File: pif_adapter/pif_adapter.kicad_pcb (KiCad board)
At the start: 2 copper layers, 11 x 22 mm, 11 parts, among them P1 Conn_02x20_Odd_Even, P10 Conn_01x01, P11 Conn_01x01, P2 PIF-NUS, P3 Conn_01x01, P4 Conn_01x01, P5 Conn_01x01, P6 Conn_01x01, P7 Conn_01x01, P8 Conn_01x01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

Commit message: - updated revision infos - changed some traces
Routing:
- net GND: track 51.8 -> 51.1 mm
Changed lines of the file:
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@@
     (thickness 1.6)
     (drawings 20)
-    (tracks 221)
+    (tracks 222)
     (zones 0)
     (modules 11)
@@
   )
   (page A4)
+  (title_block
+    (title "UltraPIF Adapter")
+    (date 2020-03-04)
+    (rev 3)
+  )
   (layers
     (0 F.Cu signal)
@@
   )
   (setup
-    (last_trace_width 0.8)
+    (last_trace_width 0.4)
     (user_trace_width 0.4)
     (user_trace_width 0.8)
@@
   (segment (start 143.03 109.25) (end 142.12 108.34) (width 0.15) (layer F.Cu) (net 9))
   (segment (start 141.01 111.225) (end 141 111.215) (width 0.15) (layer F.Cu) (net 10))
-  (segment (start 143.975 110.75) (end 142.8 110.75) (width 0.15) (layer F.Cu) (net 10))
   (segment (start 141 111.215) (end 142.035 111.215) (width 0.4) (layer F.Cu) (net 10))
   (segment (start 142.5 110.75) (end 142.8 110.75) (width 0.4) (layer F.Cu) (net 10))
   (segment (start 142.035 111.215) (end 142.5 110.75) (width 0.4) (layer F.Cu) (net 10))
-  (segment (start 143.975 108.75) (end 144.925 108.75) (width 0.15) (layer F.Cu) (net 10))
   (via (at 146.5 102.3) (size 0.6) (drill 0.4) (layers F.Cu B.Cu) (net 10))
   (segment (start 145.2 102.3) (end 146.5 102.3) (width 0.4) (layer B.Cu) (net 10))
@@
   (segment (start 143.975 103.25) (end 144.8 103.25) (width 0.15) (layer F.Cu) (net 10))
   (segment (start 145.2 102.85) (end 145.2 102.3) (width 0.15) (layer F.Cu) (net 10))
-  (segment (start 143.975 110.75) (end 145.1 110.75) (width 0.15) (layer F.Cu) (net 10))
-  (segment (start 145.1 111.25) (end 144.6 111.75) (width 0.15) (layer F.Cu) (net 10))
-  (segment (start 145.1 111.1) (end 145.1 111.25) (width 0.15) (layer F.Cu) (net 10))
-  (segment (start 144.6 111.75) (end 143.975 111.75) (width 0.15) (layer F.Cu) (net 10))
-  (segment (start 147.2 102.3) (end 146.5 102.3) (width 0.4) (layer F.Cu) (net 10))
   (segment (start 141.785 108.675) (end 142.78 109.67) (width 0.4) (layer F.Cu) (net 10))
   (segment (start 141 108.675) (end 141.785 108.675) (width 0.4) (layer F.Cu) (net 10))
-  (segment (start 142.86 109.75) (end 142.78 109.67) (width 0.15) (layer F.Cu) (net 10))
-  (segment (start 143.925 109.75) (end 142.86 109.75) (width 0.15) (layer F.Cu) (net 10))
-  (segment (start 144.75 109.75) (end 145.1 109.75) (width 0.15) (layer F.Cu) (net 10))
-  (segment (start 143.925 109.75) (end 144.75 109.75) (width 0.15) (layer F.Cu) (net 10))
   (segment (start 141.005 113.76) (end 141 113.755) (width 0.4) (layer F.Cu) (net 10))
   (segment (start 142.91 112.53) (end 141.68 113.76) (width 0.4) (layer F.Cu) (net 10))
@@
   (segment (start 142.91 112.53) (end 142.91 112.08) (width 0.4) (layer F.Cu) (net 10))
   (segment (start 142.91 112.08) (end 142.91 111.84) (width 0.15) (layer F.Cu) (net 10))
-  (segment (start 147.2 104.1) (end 145.2 104.1) (width 0.4) (layer F.Cu) (net 10))
-  (segment (start 147.212501 104.087499) (end 147.2 104.1) (width 0.4) (layer F.Cu) (net 10))
   (segment (start 145.2 104.1) (end 145.4 104.1) (width 0.15) (layer F.Cu) (net 10))
   (segment (start 143.975 104.25) (end 145.05 104.25) (width 0.15) (layer F.Cu) (net 10))
   (segment (start 145.05 104.25) (end 145.2 104.1) (width 0.15) (layer F.Cu) (net 10))
-  (segment (start 147.2 102.3) (end 147.212501 102.312501) (width 0.4) (layer F.Cu) (net 10))
   (segment (start 146.5 102.3) (end 146.5 100.1) (width 0.4) (layer F.Cu) (net 10))
   (segment (start 146.5 96.92) (end 146.5 100.1) (width 0.8) (layer F.Cu) (net 10))
   (segment (start 148 96.7) (end 146.72 96.7) (width 0.8) (layer F.Cu) (net 10))
   (segment (start 146.72 96.7) (end 146.5 96.92) (width 0.8) (layer F.Cu) (net 10))
-  (segment (start 144.02 98.21) (end 144.02 95.92501) (width 0.4) (layer F.Cu) (net 10))
-  (segment (start 143.875 98.355) (end 144.02 98.21) (width 0.4) (layer F.Cu) (net 10))
-  (segment (start 143.875 101.655) (end 143.875 98.355) (width 0.4) (layer F.Cu) (net 10))
   (segment (start 143.875 101.655) (end 143.875 102.25) (width 0.15) (layer F.Cu) (net 10))
   (segment (start 144.985 101.655) (end 145.2 101.87) (width 0.4) (layer F.Cu) (net 10))
   (segment (start 143.875 101.655) (end 144.985 101.655) (width 0.4) (layer F.Cu) (net 10))
   (segment (start 145.2 101.87) (end 145.2 102.33) (width 0.4) (layer F.Cu) (net 10))
-  (segment (start 147.175 106.835) (end 145.1 108.91) (width 0.8) (layer F.Cu) (net 10))
-  (segment (start 147.175 102.225) (end 147.175 106.835) (width 0.8) (layer F.Cu) (net 10))
-  (segment (start 146.5 100.1) (end 146.5 101.55) (width 0.8) (layer F.Cu) (net 10))
-  (segment (start 145.1 108.91) (end 145.1 110.88) (width 0.8) (layer F.Cu) (net 10))
-  (segment (start 146.5 101.55) (end 147.175 102.225) (width 0.8) (layer F.Cu) (net 10))
+  (segment (start 145.1 110.75) (end 143.975 110.75) (width 0.15) (layer F.Cu) (net 10))
+  (segment (start 143.975 110.75) (end 142.8 110.75) (width 0.15) (layer F.Cu) (net 10))
+  (segment (start 145.5 110.75) (end 145.68 110.57) (width 0.15) (layer F.Cu) (net 10))
+  (segment (start 145.1 110.75) (end 145.5 110.75) (width 0.15) (layer F.Cu) (net 10))
+  (segment (start 145.68 108.63) (end 145.68 109.78) (width 0.4) (layer F.Cu) (net 10))
+  (segment (start 145.68 109.78) (end 145.68 110.57) (width 0.4) (layer F.Cu) (net 10))
+  (segment (start 142.86 109.75) (end 142.78 109.67) (width 0.15) (layer F.Cu) (net 10))
+  (segment (start 145.68 109.78) (end 145.65 109.75) (width 0.15) (layer F.Cu) (net 10))
+  (segment (start 145.65 109.75) (end 142.86 109.75) (width 0.15) (layer F.Cu) (net 10))
+  (segment (start 145.56 108.75) (end 145.68 108.63) (width 0.15) (layer F.Cu) (net 10))
+  (segment (start 143.975 108.75) (end 145.56 108.75) (width 0.15) (layer F.Cu) (net 10))
+  (segment (start 145.48 110.87) (end 145.48 110.77) (width 0.15) (layer F.Cu) (net 10))
+  (segment (start 143.975 111.75) (end 144.6 111.75) (width 0.15) (layer F.Cu) (net 10))
+  (segment (start 144.6 111.75) (end 145.48 110.87) (width 0.15) (layer F.Cu) (net 10))
+  (segment (start 145.68 110.57) (end 145.48 110.77) (width 0.4) (layer F.Cu) (net 10))
+  (segment (start 147.17 104.1) (end 145.2 104.1) (width 0.4) (layer F.Cu) (net 10))
+  (segment (start 147.175 104.105) (end 147.17 104.1) (width 0.4) (layer F.Cu) (net 10))
+  (segment (start 147.175 107.135) (end 145.68 108.63) (width 0.4) (layer F.Cu) (net 10))
+  (segment (start 146.5 102.3) (end 147.175 102.975) (width 0.4) (layer F.Cu) (net 10))
+  (segment (start 147.175 102.975) (end 147.175 107.135) (width 0.4) (layer F.Cu) (net 10))
+  (segment (start 143.875 98.355) (end 144.02 98.21) (width 0.4) (layer F.Cu) (net 10))
+  (segment (start 143.875 101.655) (end 143.875 98.355) (width 0.4) (layer F.Cu) (net 10))
+  (segment (start 144.02 98.21) (end 144.02 95.92501) (width 0.4) (layer F.Cu) (net 10))
   (segment (start 141.85 109.95) (end 141.005 109.95) (width 0.15) (layer F.Cu) (net 11))
   (segment (start 141.005 109.95) (end 141 109.945) (width 0.15) (layer F.Cu) (net 11))

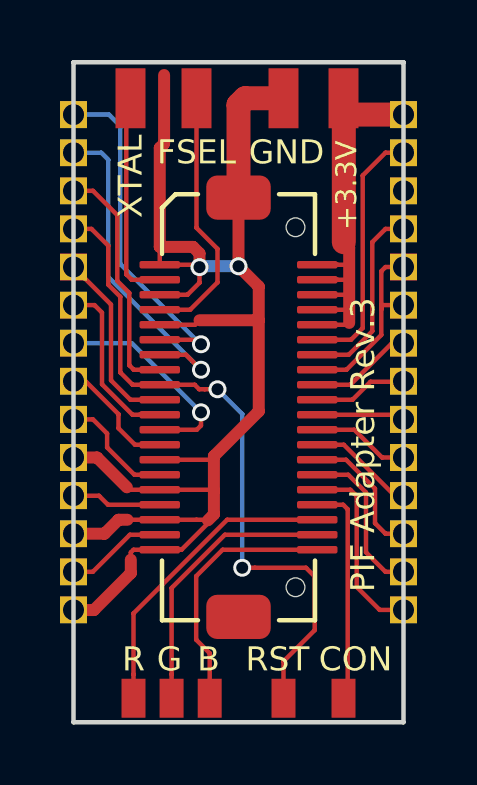
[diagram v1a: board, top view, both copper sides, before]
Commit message: improved ground trace
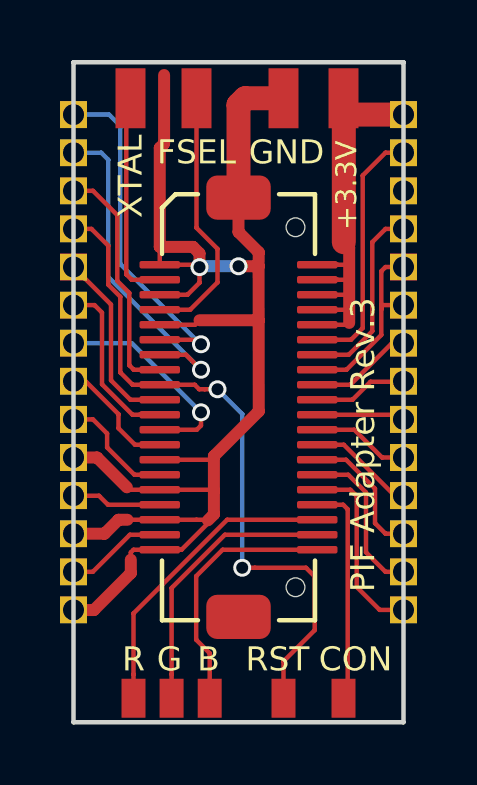
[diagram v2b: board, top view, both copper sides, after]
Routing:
- net GND: track 51.1 -> 51.8 mm
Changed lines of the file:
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@@
     (thickness 1.6)
     (drawings 20)
-    (tracks 222)
+    (tracks 224)
     (zones 0)
     (modules 11)
@@
   (segment (start 143.975 104.25) (end 145.05 104.25) (width 0.15) (layer F.Cu) (net 10))
   (segment (start 145.05 104.25) (end 145.2 104.1) (width 0.15) (layer F.Cu) (net 10))
-  (segment (start 146.5 102.3) (end 146.5 100.1) (width 0.4) (layer F.Cu) (net 10))
   (segment (start 146.5 96.92) (end 146.5 100.1) (width 0.8) (layer F.Cu) (net 10))
   (segment (start 148 96.7) (end 146.72 96.7) (width 0.8) (layer F.Cu) (net 10))
@@
   (segment (start 147.17 104.1) (end 145.2 104.1) (width 0.4) (layer F.Cu) (net 10))
   (segment (start 147.175 104.105) (end 147.17 104.1) (width 0.4) (layer F.Cu) (net 10))
-  (segment (start 147.175 107.135) (end 145.68 108.63) (width 0.4) (layer F.Cu) (net 10))
-  (segment (start 146.5 102.3) (end 147.175 102.975) (width 0.4) (layer F.Cu) (net 10))
-  (segment (start 147.175 102.975) (end 147.175 107.135) (width 0.4) (layer F.Cu) (net 10))
   (segment (start 143.875 98.355) (end 144.02 98.21) (width 0.4) (layer F.Cu) (net 10))
   (segment (start 143.875 101.655) (end 143.875 98.355) (width 0.4) (layer F.Cu) (net 10))
   (segment (start 144.02 98.21) (end 144.02 95.92501) (width 0.4) (layer F.Cu) (net 10))
+  (segment (start 145.68 108.63) (end 147.175 107.135) (width 0.4) (layer F.Cu) (net 10))
+  (segment (start 146.5 102.3) (end 147.17 102.3) (width 0.4) (layer F.Cu) (net 10))
+  (segment (start 147.175 107.135) (end 147.17 102.3) (width 0.4) (layer F.Cu) (net 10))
+  (segment (start 146.5 101.16) (end 146.5 100.1) (width 0.4) (layer F.Cu) (net 10))
+  (segment (start 147.17 102.3) (end 147.175 101.835) (width 0.4) (layer F.Cu) (net 10))
+  (segment (start 147.175 101.835) (end 146.5 101.16) (width 0.4) (layer F.Cu) (net 10))
   (segment (start 141.85 109.95) (end 141.005 109.95) (width 0.15) (layer F.Cu) (net 11))
   (segment (start 141.005 109.95) (end 141 109.945) (width 0.15) (layer F.Cu) (net 11))
